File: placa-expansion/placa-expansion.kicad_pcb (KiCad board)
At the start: 2 copper layers, 70 x 114.2 mm, 24 parts, among them J1 PBD-26, P1 BATT, P2 CONN_3PI, P3 PWR_HUB, P4 PWR_3pi, P5 CONN_4, P6 CONN_4, P7 CONN_4, P8 CONN_4, U1 PTN78020

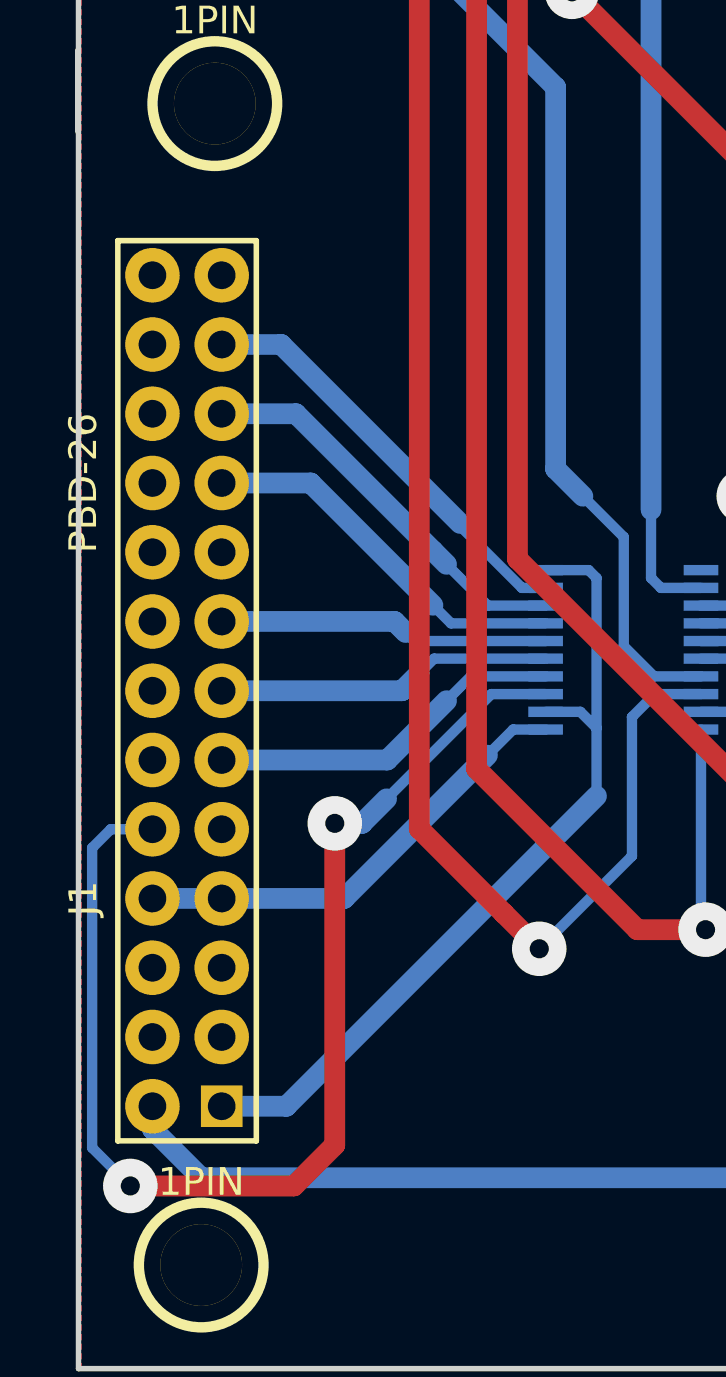
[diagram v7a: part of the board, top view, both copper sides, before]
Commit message: subo nueva version del diseño del pcb, corregido J1
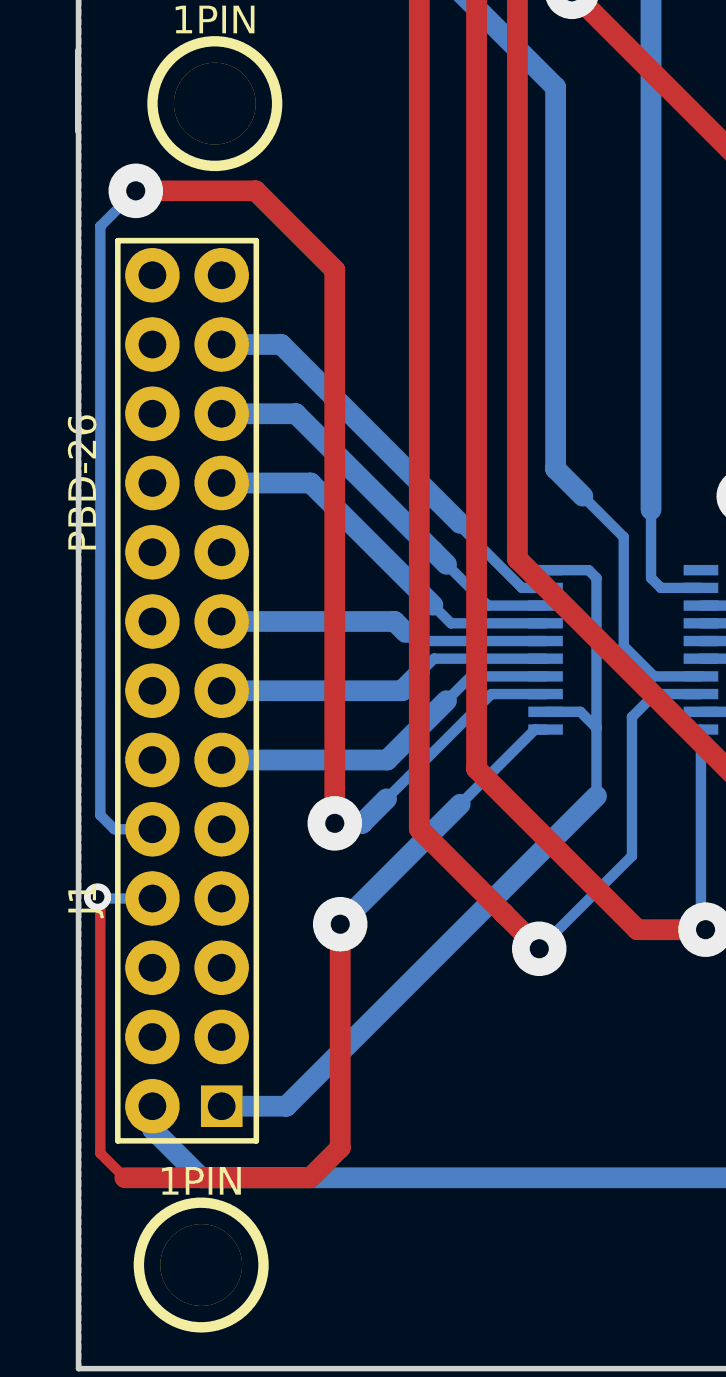
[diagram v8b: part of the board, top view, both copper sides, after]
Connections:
- J1 pad 12: (no net) -> N-000004
- J1 pad 14: (no net) -> N-0000029
- J1 pad 16: (no net) -> N-0000010
- J1 pad 17: (no net) -> N-0000026
- J1 pad 18: (no net) -> N-0000011
- J1 pad 20: (no net) -> N-0000018
- J1 pad 22: (no net) -> N-0000012
- J1 pad 24: (no net) -> N-0000013
- J1 pad 25: (no net) -> N-0000027
- J1 pad 26: (no net) -> N-0000014
- J1 pad 3: (no net) -> N-0000016
- J1 pad 4: (no net) -> N-0000022
- J1 pad 5: (no net) -> N-0000015
- J1 pad 7: /TX_rPi -> N-0000021
- J1 pad 9: (no net) -> N-0000020
- P2 pad 3: (no net) -> /VBoost
- P2 pad 5: (no net) -> /Vbat_3pi
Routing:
- net /TX_rPi: track 17.0 -> 39.8 mm, vias 0 -> 2
- net /RX_rPi: track 46.4 -> 65.3 mm
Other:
- net class Default: clearance 0.508 -> 0.254; trace_width 0.762 -> 0.381
- rule trace_clearance: 0.508 -> 0.254
